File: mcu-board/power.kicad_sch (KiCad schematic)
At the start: 15 parts, among them Q1 SSM3J328R,LF, Q2 SSM3J328R,LF, U2 L7806, U3 L7806, U4 AZ1117-3.3

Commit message: finished schematic(?)
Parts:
- added J6, J7, J8: Conn_01x02, Connector_JST:JST_PH_B2B-PH-K_1x02_P2.00mm_Vertical, symbol Connector_Generic:Conn_01x02
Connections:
- net +BATT: now also J6.2 (Pin_2)
- net GND: now also J8.1 (Pin_1)
- new net: J6.1 (Pin_1), J7.2 (Pin_2)
- new net: J7.1 (Pin_1), J8.2 (Pin_2)
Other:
- note added: "Battery Connectors"

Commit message: footprints
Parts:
- C1, C2, C3, C4: footprint Capacitor_SMD:C_1206_3216Metric -> Capacitor_SMD:C_0603_1608Metric
- C5, C6: footprint Capacitor_SMD:C_1206_3216Metric -> Capacitor_SMD:C_0805_2012Metric
- R3: footprint Resistor_SMD:R_1206_3216Metric -> Resistor_SMD:R_0603_1608Metric
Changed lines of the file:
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@@
 		(dnp no)
 		(fields_autoplaced yes)
-		(property "Reference" "#PWR?"
+		(property "Reference" "#PWR0107"
 			(at 124.46 82.55 0)
 			(effects
@@
 			(project "mcu board"
 				(path "/e926887c-cd26-4f47-be51-3352b14f6743/65b6e221-2db7-4e52-96fb-70ae76f49758"
-					(reference "#PWR?")
+					(reference "#PWR0107")
 					(unit 1)
 				)
@@
 		(dnp no)
 		(fields_autoplaced yes)
-		(property "Reference" "#PWR?"
+		(property "Reference" "#PWR0102"
 			(at 187.96 82.55 0)
 			(effects
@@
 			(project "mcu board"
 				(path "/e926887c-cd26-4f47-be51-3352b14f6743/65b6e221-2db7-4e52-96fb-70ae76f49758"
-					(reference "#PWR?")
+					(reference "#PWR0102")
 					(unit 1)
 				)
@@
 			)
 		)
-		(property "Footprint" "Capacitor_SMD:C_1206_3216Metric"
+		(property "Footprint" "Capacitor_SMD:C_0603_1608Metric"
 			(at 116.84 90.17 0)
 			(effects
@@
 		(dnp no)
 		(fields_autoplaced yes)
-		(property "Reference" "#PWR?"
+		(property "Reference" "#PWR0103"
 			(at 179.07 133.35 0)
 			(effects
@@
 			(project "mcu board"
 				(path "/e926887c-cd26-4f47-be51-3352b14f6743/65b6e221-2db7-4e52-96fb-70ae76f49758"
-					(reference "#PWR?")
+					(reference "#PWR0103")
 					(unit 1)
 				)
@@
 		(dnp no)
 		(fields_autoplaced yes)
-		(property "Reference" "#PWR?"
+		(property "Reference" "#PWR0112"
 			(at 264.16 82.55 0)
 			(effects
@@
 			(project "mcu board"
 				(path "/e926887c-cd26-4f47-be51-3352b14f6743/65b6e221-2db7-4e52-96fb-70ae76f49758"
-					(reference "#PWR?")
+					(reference "#PWR0112")
 					(unit 1)
 				)
@@
 		(dnp no)
 		(fields_autoplaced yes)
-		(property "Reference" "#PWR?"
+		(property "Reference" "#PWR0110"
 			(at 209.55 133.35 0)
 			(effects
@@
 			(project "mcu board"
 				(path "/e926887c-cd26-4f47-be51-3352b14f6743/65b6e221-2db7-4e52-96fb-70ae76f49758"
-					(reference "#PWR?")
+					(reference "#PWR0110")
 					(unit 1)
 				)
@@
 		(dnp no)
 		(fields_autoplaced yes)
-		(property "Reference" "#PWR?"
+		(property "Reference" "#PWR0101"
 			(at 139.7 82.55 0)
 			(effects
@@
 			(project "mcu board"
 				(path "/e926887c-cd26-4f47-be51-3352b14f6743/65b6e221-2db7-4e52-96fb-70ae76f49758"
-					(reference "#PWR?")
+					(reference "#PWR0101")
 					(unit 1)
 				)
@@
 		(dnp no)
 		(fields_autoplaced yes)
-		(property "Reference" "#PWR?"
+		(property "Reference" "#PWR0111"
 			(at 276.86 82.55 0)
 			(effects
@@
 			(project "mcu board"
 				(path "/e926887c-cd26-4f47-be51-3352b14f6743/65b6e221-2db7-4e52-96fb-70ae76f49758"
-					(reference "#PWR?")
+					(reference "#PWR0111")
 					(unit 1)
 				)
@@
 			)
 		)
-		(property "Footprint" "Capacitor_SMD:C_1206_3216Metric"
+		(property "Footprint" "Capacitor_SMD:C_0603_1608Metric"
 			(at 116.84 115.57 0)
 			(effects
@@
 			)
 		)
-		(property "Footprint" "Capacitor_SMD:C_1206_3216Metric"
+		(property "Footprint" "Capacitor_SMD:C_0603_1608Metric"
 			(at 73.66 90.17 0)
 			(effects
@@
 		(dnp no)
 		(fields_autoplaced yes)
-		(property "Reference" "#PWR?"
+		(property "Reference" "#PWR0108"
 			(at 228.6 82.55 0)
 			(effects
@@
 			(project "mcu board"
 				(path "/e926887c-cd26-4f47-be51-3352b14f6743/65b6e221-2db7-4e52-96fb-70ae76f49758"
-					(reference "#PWR?")
+					(reference "#PWR0108")
 					(unit 1)
 				)
@@
 		(dnp no)
 		(fields_autoplaced yes)
-		(property "Reference" "#PWR?"
+		(property "Reference" "#PWR0106"
 			(at 114.3 133.35 0)
 			(effects
@@
 			(project "mcu board"
 				(path "/e926887c-cd26-4f47-be51-3352b14f6743/65b6e221-2db7-4e52-96fb-70ae76f49758"
-					(reference "#PWR?")
+					(reference "#PWR0106")
 					(unit 1)
 				)
@@
 			)
 		)
-		(property "Footprint" "Resistor_SMD:R_1206_3216Metric"
+		(property "Footprint" "Resistor_SMD:R_0603_1608Metric"
 			(at 209.55 97.79 0)
 			(effects
@@
 			)
 		)
-		(property "Footprint" "Capacitor_SMD:C_1206_3216Metric"
+		(property "Footprint" "Capacitor_SMD:C_0603_1608Metric"
 			(at 73.66 115.57 0)
 			(effects
@@
 			)
 		)
-		(property "Footprint" "Capacitor_SMD:C_1206_3216Metric"
+		(property "Footprint" "Capacitor_SMD:C_0805_2012Metric"
 			(at 147.32 90.17 0)
 			(effects
@@
 		(dnp no)
 		(fields_autoplaced yes)
-		(property "Reference" "#PWR?"
+		(property "Reference" "#PWR0104"
 			(at 24.13 82.55 0)
 			(effects
@@
 			(project "mcu board"
 				(path "/e926887c-cd26-4f47-be51-3352b14f6743/65b6e221-2db7-4e52-96fb-70ae76f49758"
-					(reference "#PWR?")
+					(reference "#PWR0104")
 					(unit 1)
 				)
@@
 		(dnp no)
 		(fields_autoplaced yes)
-		(property "Reference" "#PWR?"
+		(property "Reference" "#PWR0105"
 			(at 46.99 82.55 0)
 			(effects
@@
 			(project "mcu board"
 				(path "/e926887c-cd26-4f47-be51-3352b14f6743/65b6e221-2db7-4e52-96fb-70ae76f49758"
-					(reference "#PWR?")
+					(reference "#PWR0105")
 					(unit 1)
 				)
@@
 		(dnp no)
 		(fields_autoplaced yes)
-		(property "Reference" "#PWR?"
+		(property "Reference" "#PWR0109"
 			(at 242.57 82.55 0)
 			(effects
@@
 			(project "mcu board"
 				(path "/e926887c-cd26-4f47-be51-3352b14f6743/65b6e221-2db7-4e52-96fb-70ae76f49758"
-					(reference "#PWR?")
+					(reference "#PWR0109")
 					(unit 1)
 				)
@@
 			)
 		)
-		(property "Footprint" "Capacitor_SMD:C_1206_3216Metric"
+		(property "Footprint" "Capacitor_SMD:C_0805_2012Metric"
 			(at 179.07 90.17 0)
 			(effects

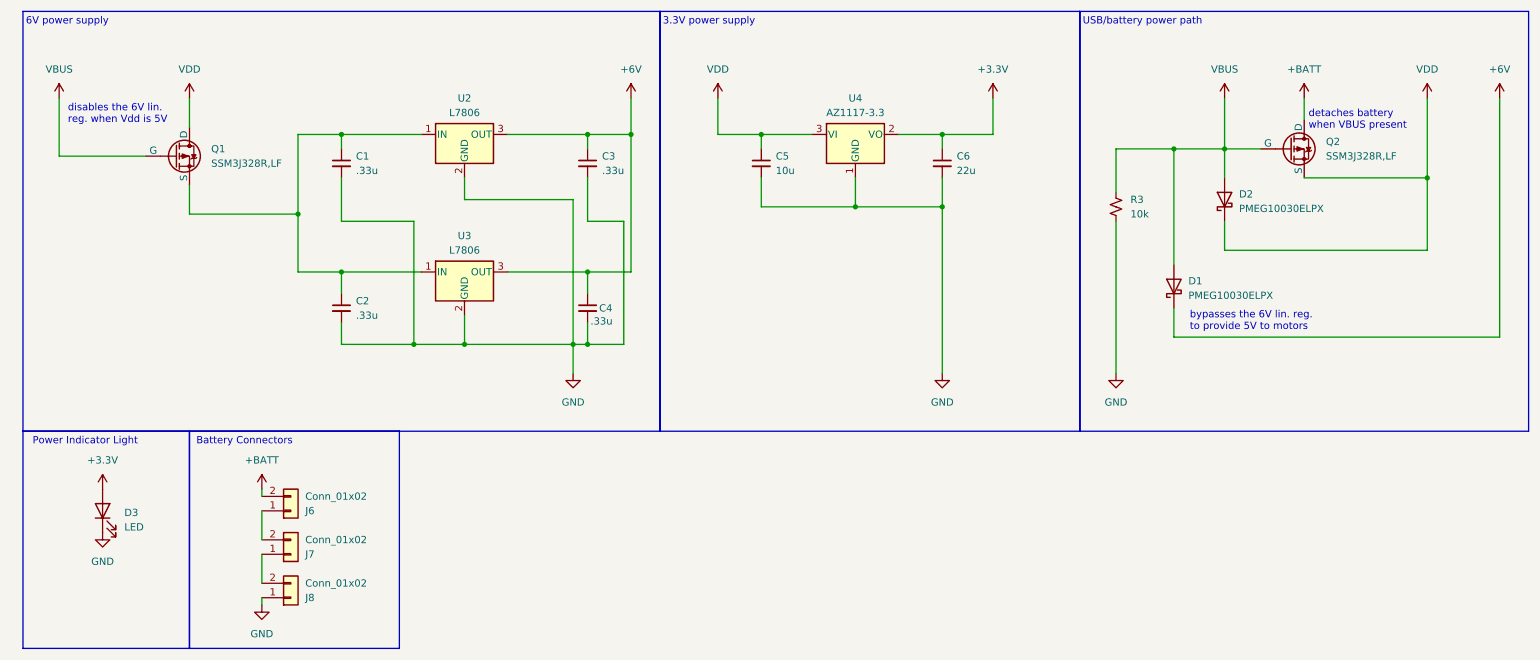
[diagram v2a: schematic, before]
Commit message: pcb routed
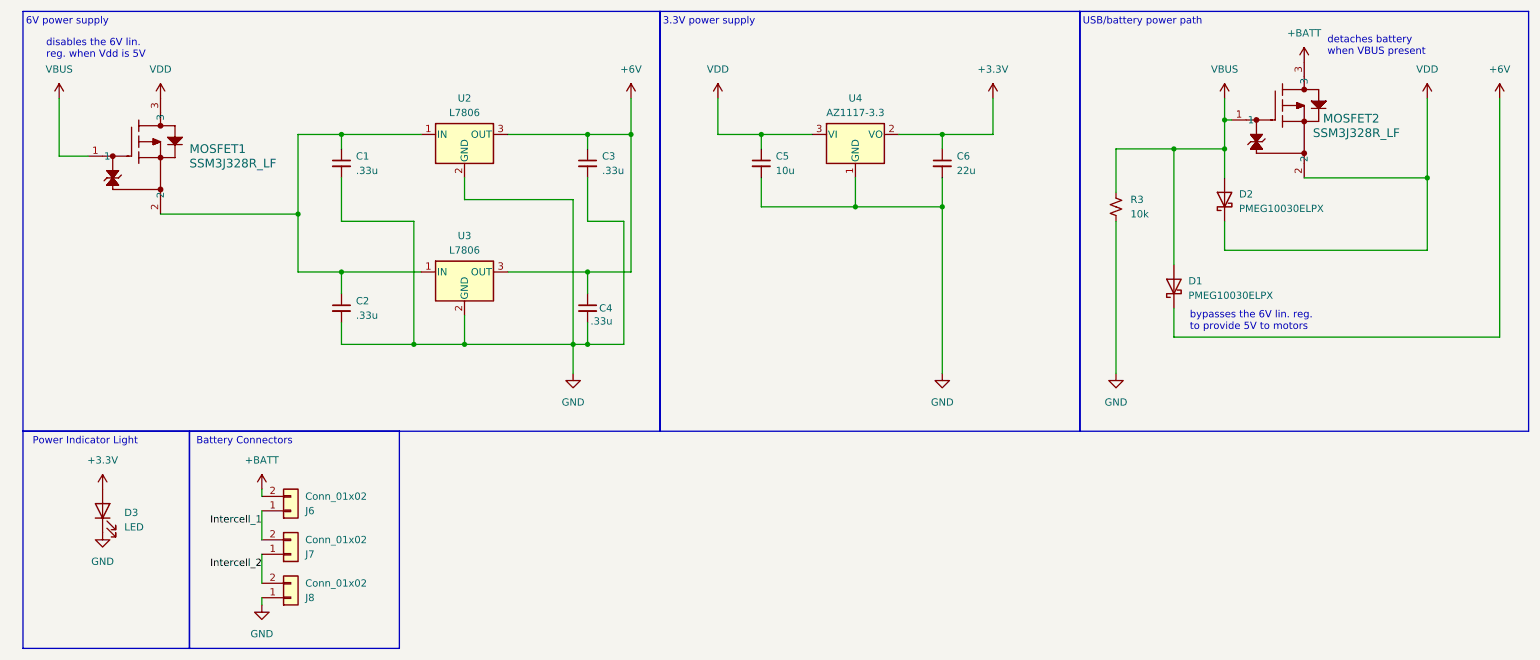
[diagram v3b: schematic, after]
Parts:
- removed Q1, Q2: SSM3J328R,LF, Package_TO_SOT_SMD:SOT-23, symbol Simulation_SPICE:PMOS
- added MOSFET1, MOSFET2: SSM3J328R_LF, SOT-23F_TOS, symbol ssm3j3:SSM3J328R_LF
- D3: footprint (none) -> LED_SMD:LED_0603_1608Metric
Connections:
- net +BATT: now also MOSFET2.3
- net VBUS: now also MOSFET1.1, MOSFET2.1
- net VDD: now also MOSFET1.3, MOSFET2.2
- net at C1.1, C2.1, U2.1 (IN)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: now also MOSFET1.2
- net Intercell_1: now reaches J6.1 (Pin_1), J7.2 (Pin_2)
- net Intercell_2: now reaches J7.1 (Pin_1), J8.2 (Pin_2)
